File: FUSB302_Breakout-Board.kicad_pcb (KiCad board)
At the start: 2 copper layers, 20 x 20 mm, 3 parts, among them J1 Conn_01x07_Male, J2 Conn_01x07_Male, U1 FUSB302BMPX

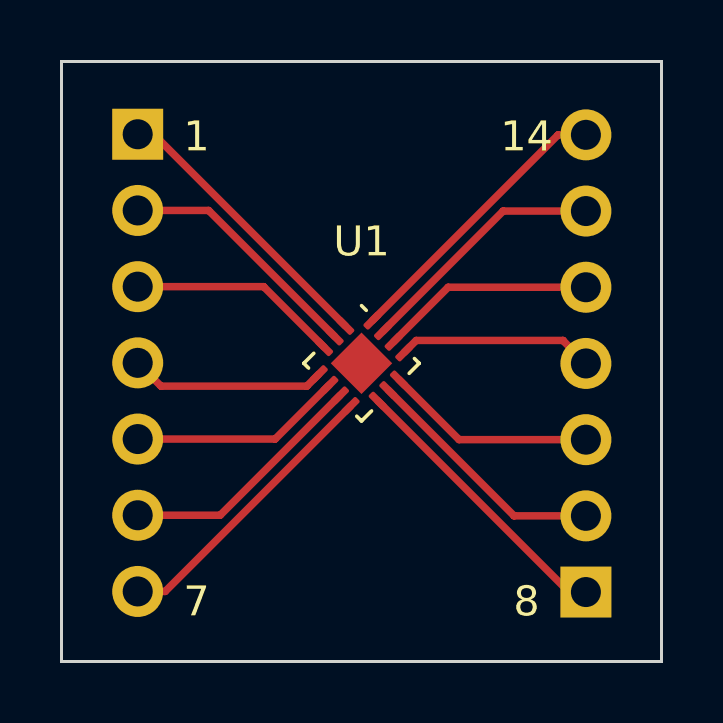
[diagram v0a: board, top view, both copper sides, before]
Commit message: Mod: PCB, added vias to filled zone on the bottom for a better heat path Mod: Panel, with new pcb Mod: Exports
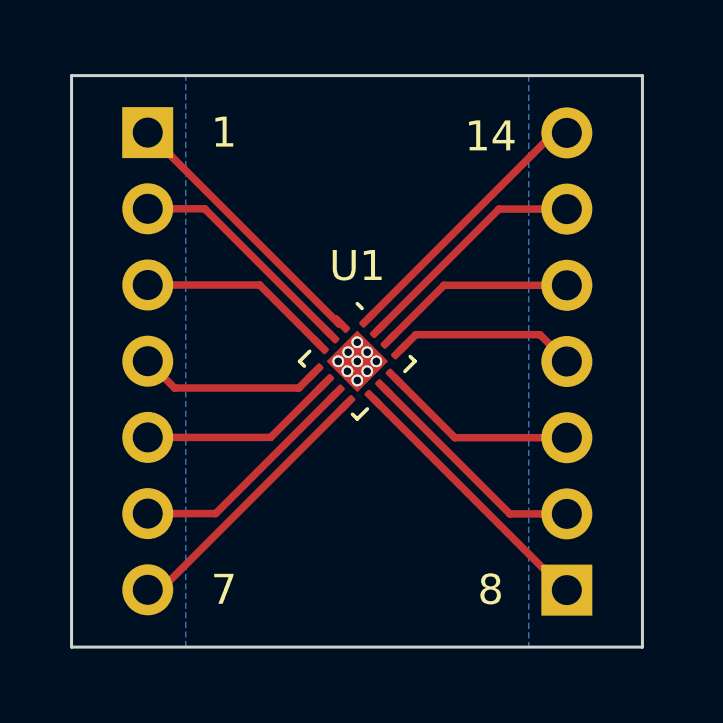
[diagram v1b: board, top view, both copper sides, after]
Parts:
- moved J2 0.64 mm to (156.8, 122.6)
- moved J1 0.34 mm to (142.9, 107.3)
- moved U1 0.15 mm to (149.9, 114.9)
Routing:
- net GND: track 17.9 -> 16.9 mm, vias 0 -> 9
- net VCONN: track 15.6 -> 14.6 mm
- net CC2: track 19.2 -> 18.3 mm
- net CC1: track 13.6 -> 12.7 mm
- net VDD: track 13.6 -> 12.7 mm
- added copper zone on B.Cu, net GND
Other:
- board size 20 x 20 mm -> 19 x 19 mm

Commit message: Mod: Bottom solder mask, pasted logo in to it and exported the pcb with the v-cuts
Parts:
- added G***: LOGO, drawings:elektronik-emblem_3x3.5_solder, B.Cu at (149.9, 109.2)

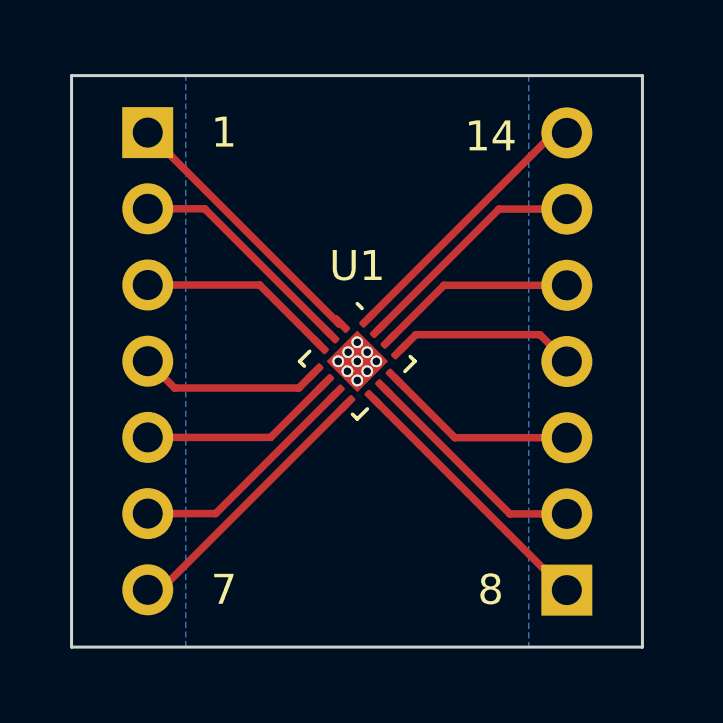
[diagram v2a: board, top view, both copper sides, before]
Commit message: Mod: Corrected trace to first pin, added Rev. and Prj. to the bottom solder mask
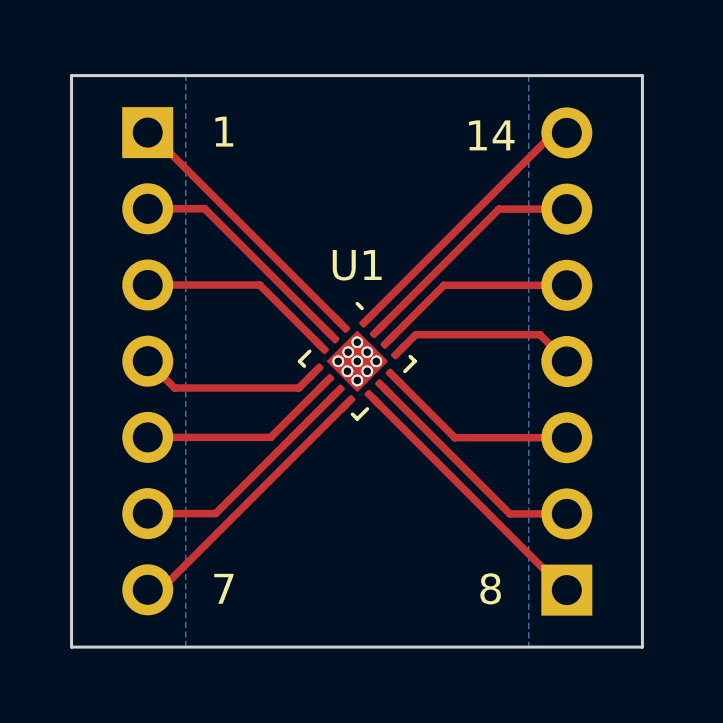
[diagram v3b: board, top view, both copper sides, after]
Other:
- board text added: "Prj: ${TITLE} Rev: ${REVISION}"
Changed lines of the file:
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@@
     (effects (font (size 1 1) (thickness 0.15)))
+  )
+  (gr_text "Prj: ${TITLE}\nRev: ${REVISION}" (at 149.86 120.65) (layer "B.Mask")
+    (effects (font (size 0.4 0.4) (thickness 0.1)) (justify mirror))
   )
   (segment (start 156.845 114.94) (end 155.951 114.046) (width 0.25) (layer "F.Cu") (net 1))
@@
   (segment (start 156.845 109.86) (end 154.581447 109.86) (width 0.25) (layer "F.Cu") (net 8))
   (segment (start 154.581447 109.86) (end 150.575946 113.865501) (width 0.25) (layer "F.Cu") (net 8))
-  (segment (start 149.253724 113.688724) (end 149.320831 113.688724) (width 0.25) (layer "F.Cu") (net 9))
-  (segment (start 142.875 107.31) (end 149.253724 113.688724) (width 0.25) (layer "F.Cu") (net 9))
+  (segment (start 142.942107 107.31) (end 149.320831 113.688724) (width 0.25) (layer "F.Cu") (net 9))
   (segment (start 156.845 107.32) (end 156.41434 107.32) (width 0.25) (layer "F.Cu") (net 9))
   (segment (start 156.41434 107.32) (end 150.222392 113.511948) (width 0.25) (layer "F.Cu") (net 9))
+  (segment (start 142.875 107.31) (end 142.942107 107.31) (width 0.25) (layer "F.Cu") (net 9))
   (zone (net 7) (net_name "GND") (layer "B.Cu") (hatch edge 0.508)
     (connect_pads (clearance 0.508))
